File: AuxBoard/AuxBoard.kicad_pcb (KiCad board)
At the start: 2 copper layers, 85.2 x 59.2 mm, 29 parts, among them J1 ATX-24, J10 MatBIn, J11 FanHeader, J2 RPI4B, J4 MatrixASupply, J5 MatrixBSupply, J6 BigLED, J7 MatAOut, J8 MatAIn, J9 MatBOut, Q1 DMMT5401, Q2 DMG2305UX, Q3 DMG2305UX, Q4 DMG2305UX, SW1 SW_DPST, U1 74AHC04

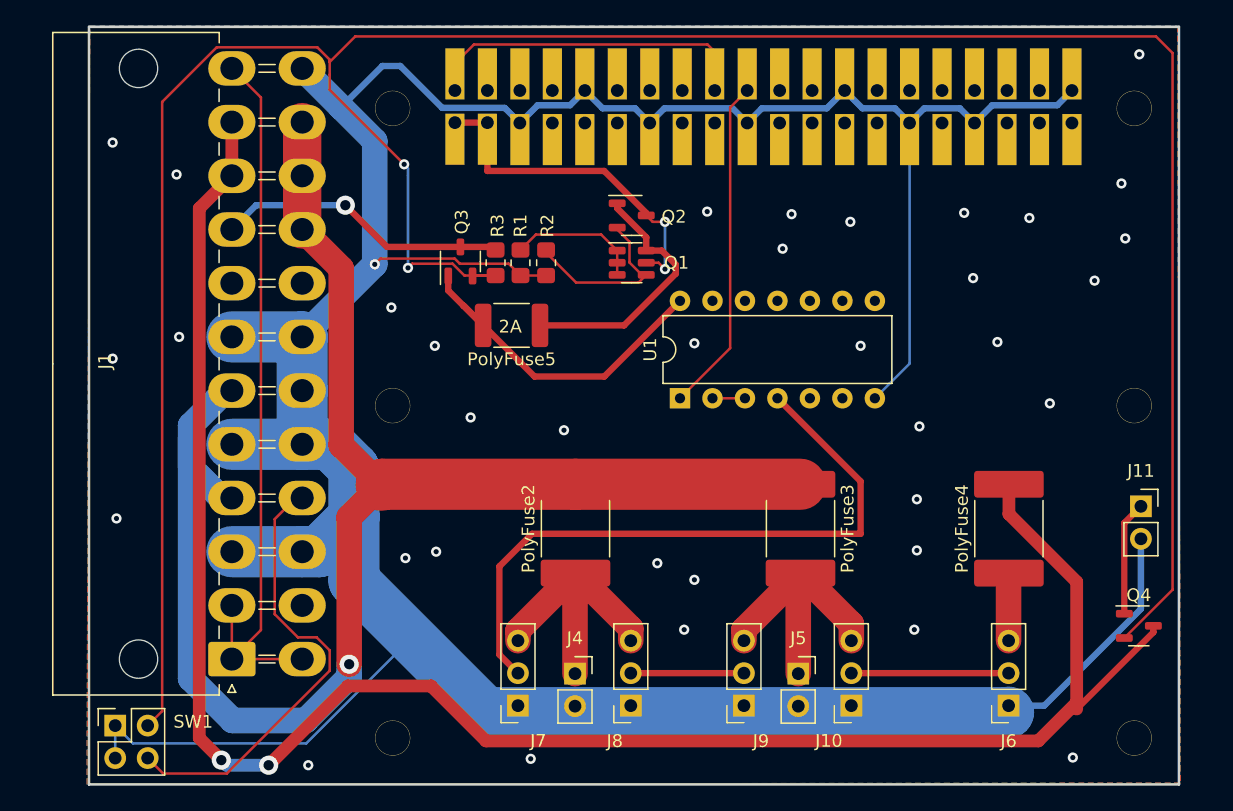
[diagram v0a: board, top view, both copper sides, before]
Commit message: Added Silkscreen
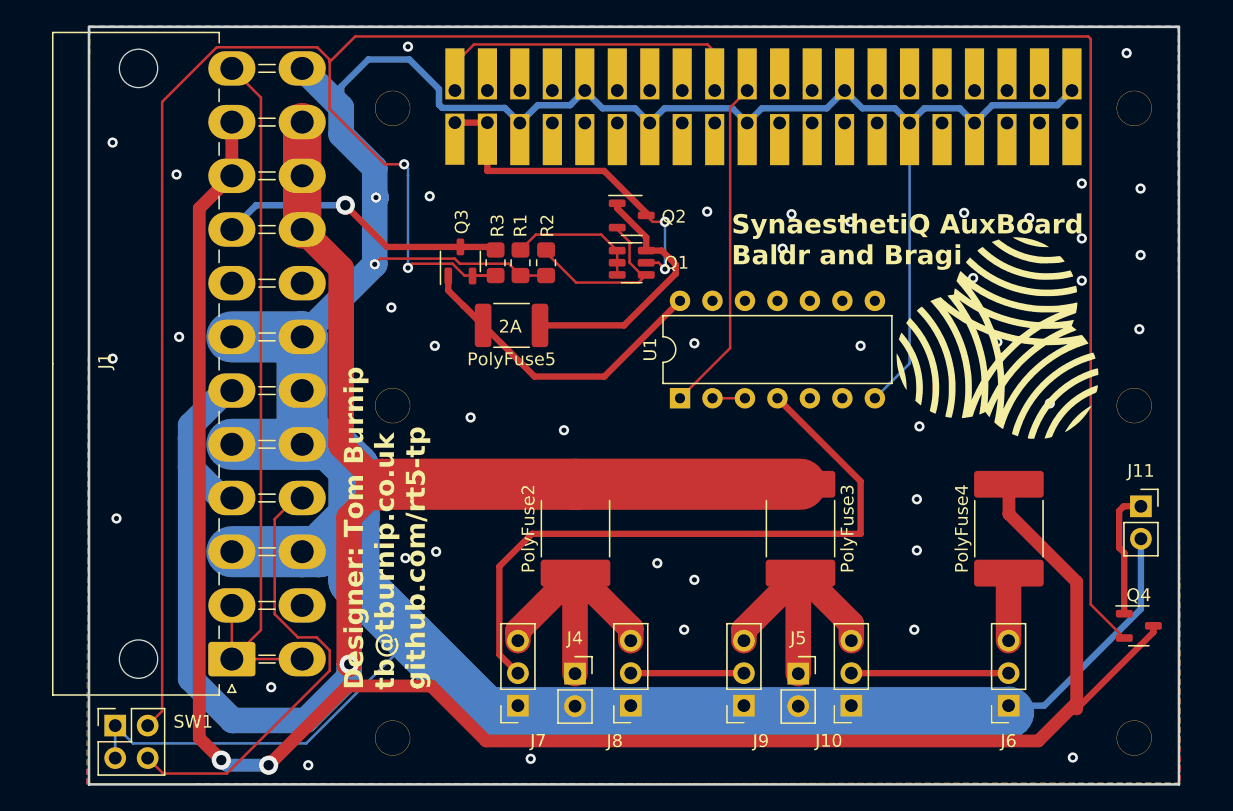
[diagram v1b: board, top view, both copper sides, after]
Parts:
- added G***: LOGO, RTEP:RTEPLogo, F.Cu at (175.8, 74.1)
- added G***: LOGO, RTEP:RTEPLogo, B.Cu at (175.5, 77.1)
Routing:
- net /5VSwitch: track 207.1 -> 201.8 mm
- net GND: track 278.1 -> 280.2 mm, vias 37 -> 44
- net Net-(J11-Pin_1): track 8.94 -> 10.1 mm
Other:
- board text added: "Designer: Tom Burnip tb@tburnip.co.uk github.com/rt5-tp"
- board text added: "SynaesthetiQ AuxBoard Baldr and Bragi"
- board text added: "SynaesthetiQ AuxBoard Baldr and Bragi Designer: Tom Burnip (tb@tburnip.co.uk) GitHub: https://github.com/rt5-tp"

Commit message: Gerbers for PCB. Fixed RPI Header Mistake. PCB will need bodge.
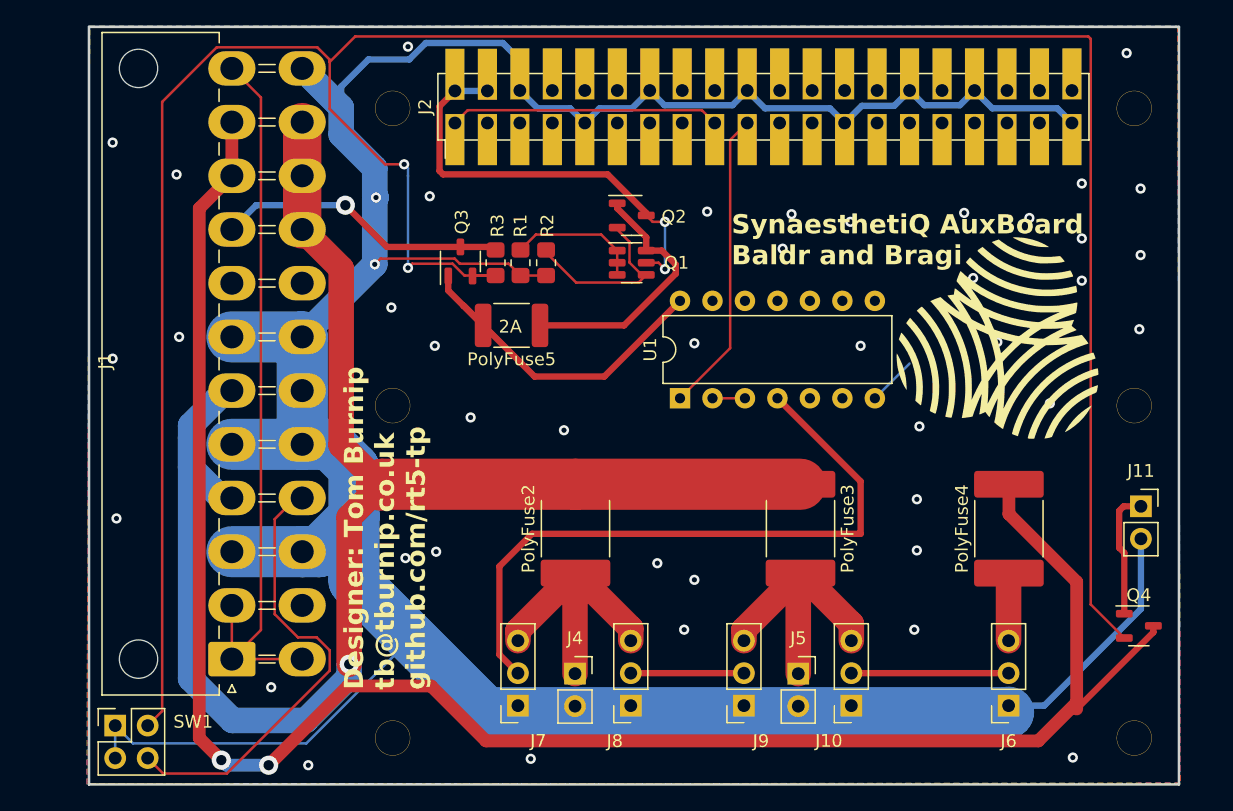
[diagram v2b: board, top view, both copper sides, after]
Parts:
- J1: footprint Connector_Molex:Molex_Mini-Fit_Jr_5569-24A2_2x12_P4.20mm_Horizontal -> Tom's Parts:Molex_Mini-Fit_Jr_5569-24A2_2x12_P4.20mm_Horizontal
- J2: moved to F.Cu
- turned J2 to 90 degrees
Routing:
- net GND: track 280.2 -> 262.1 mm
- net /5V_Power: track 27.3 -> 34.1 mm
- net /3V3_Power: track 26.3 -> 21.1 mm
- net /MOSI: track 26.2 -> 23.7 mm

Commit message: Fixing Header Orientation
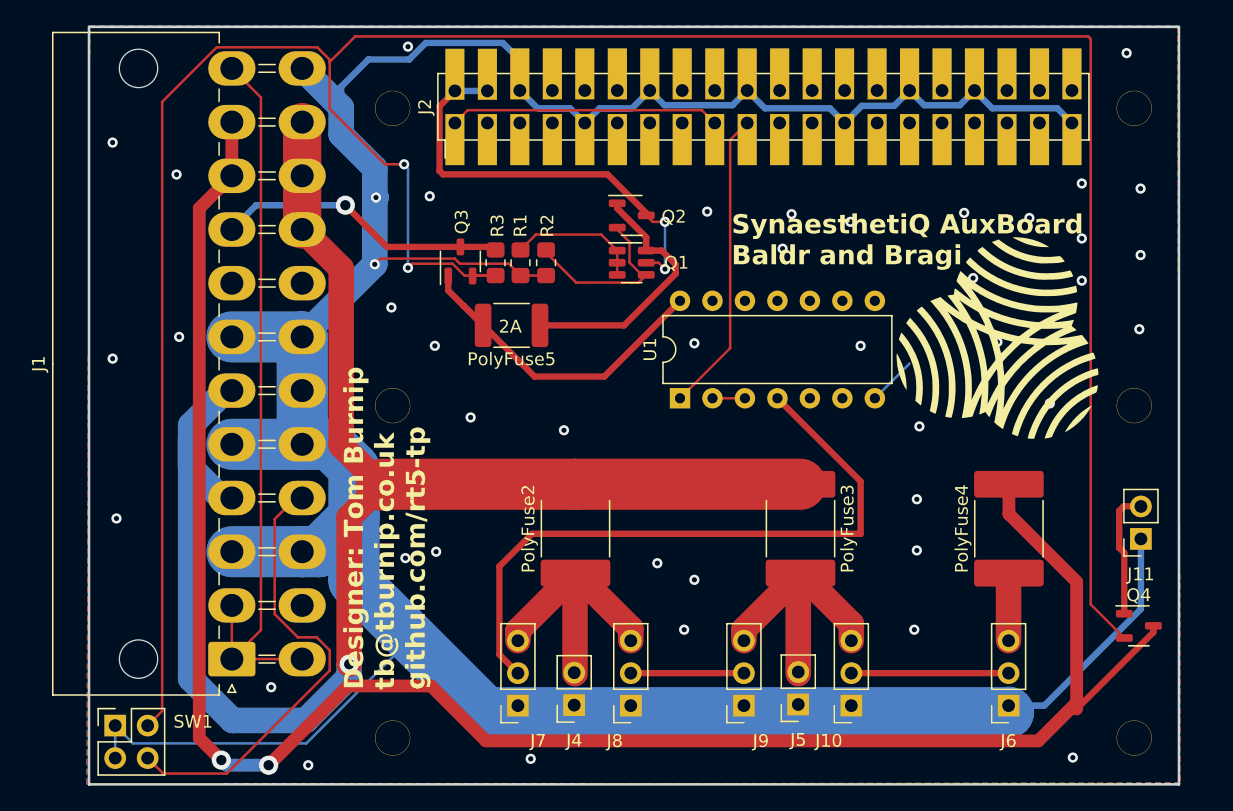
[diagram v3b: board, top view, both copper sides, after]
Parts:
- J1: footprint Tom's Parts:Molex_Mini-Fit_Jr_5569-24A2_2x12_P4.20mm_Horizontal -> Connector_Molex:Molex_Mini-Fit_Jr_5569-24A2_2x12_P4.20mm_Horizontal
- moved J11 2.55 mm to (187.0, 89.8), turned to 180 degrees
- moved J4 2.46 mm to (142.7, 102.8), turned to 180 degrees
- moved J5 2.41 mm to (160.2, 102.8), turned to 180 degrees
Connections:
- J11 pad 1: Net-(J11-Pin_1) -> GND
- J11 pad 2: GND -> Net-(J11-Pin_2)
- J4 pad 1: 5VMatA -> GND
- J4 pad 2: GND -> 5VMatA
- J5 pad 1: 5VMatB -> GND
- J5 pad 2: GND -> 5VMatB
- Q4 pad 1: Net-(J11-Pin_1) -> Net-(J11-Pin_2)
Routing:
- net Net-(J11-Pin_2): track 0.00 -> 10.1 mm
- net Net-(J11-Pin_1): track 10.1 -> 0.00 mm
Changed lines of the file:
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@@
   (net 48 "GND")
   (net 49 "+5VP")
-  (net 50 "Net-(J11-Pin_1)")
+  (net 50 "Net-(J11-Pin_2)")
   (net 51 "unconnected-(U1-Pad8)")
   (net 52 "unconnected-(U1-Pad9)")
@@
     )
   )
-  (footprint "Tom's Parts:Molex_Mini-Fit_Jr_5569-24A2_2x12_P4.20mm_Horizontal" (layer "F.Cu")
+  (footprint "Connector_Molex:Molex_Mini-Fit_Jr_5569-24A2_2x12_P4.20mm_Horizontal" (layer "F.Cu")
     (at 115.925 99.2 90)
     (descr "Molex Mini-Fit Jr. Power Connectors, old mpn/engineering number: 5569-24A2, example for new mpn: 39-30-0240, 12 Pins per row, Mounting: Snap-in Plastic Peg PCB Lock (http://www.molex.com/pdm_docs/sd/039300020_sd.pdf), generated with kicad-footprint-generator")
@@
     (property "ki_keywords" "ATX PSU")
     (attr through_hole)
-    (fp_text reference "J1" (at 23.3 -9.925 90) (layer "F.SilkS")
+    (fp_text reference "J1" (at 23.1 -15.1 90) (layer "F.SilkS")
         (effects (font (size 1 1) (thickness 0.15)))
     )
@@
         (effects (font (size 1 1) (thickness 0.15)))
     )
-    (fp_text user "${REFERENCE}" (at 23.6 -8.525 90) (layer "F.Fab")
+    (fp_text user "${REFERENCE}" (at 23.1 -13.2 90) (layer "F.Fab")
         (effects (font (size 1 1) (thickness 0.15)))
     )
-    (fp_line (start -2.81 -10.16) (end 23.1 -10.16)
+    (fp_line (start -2.81 -14.01) (end 23.1 -14.01)
       (stroke (width 0.12) (type solid)) (layer "F.SilkS"))
-    (fp_line (start -2.81 -0.99) (end -2.81 -10.16)
+    (fp_line (start -2.81 -0.99) (end -2.81 -14.01)
       (stroke (width 0.12) (type solid)) (layer "F.SilkS"))
     (fp_line (start -2.6 -0.3) (end -2 0)
@@
     (fp_line (start 48.2 -0.99) (end 49.01 -0.99)
       (stroke (width 0.12) (type solid)) (layer "F.SilkS"))
-    (fp_line (start 49.01 -10.16) (end 23.1 -10.16)
+    (fp_line (start 49.01 -14.01) (end 23.1 -14.01)
       (stroke (width 0.12) (type solid)) (layer "F.SilkS"))
-    (fp_line (start 49.01 -0.99) (end 49.01 -10.16)
+    (fp_line (start 49.01 -0.99) (end 49.01 -14.01)
       (stroke (width 0.12) (type solid)) (layer "F.SilkS"))
     (fp_line (start -3.2 -14.4) (end -3.2 7.85)
@@
     (fp_line (start 49.4 7.85) (end 49.4 -14.4)
       (stroke (width 0.05) (type solid)) (layer "F.CrtYd"))
-    (fp_line (start -2.7 -10.16) (end -2.7 -1.1)
+    (fp_line (start -2.7 -13.9) (end -2.7 -1.1)
       (stroke (width 0.1) (type solid)) (layer "F.Fab"))
     (fp_line (start -2.7 -1.1) (end 48.9 -1.1)
@@
     (fp_line (start 0 -2.514214) (end 1 -1.1)
       (stroke (width 0.1) (type solid)) (layer "F.Fab"))
-    (fp_line (start 48.9 -10.16) (end -2.7 -10.16)
+    (fp_line (start 48.9 -13.9) (end -2.7 -13.9)
       (stroke (width 0.1) (type solid)) (layer "F.Fab"))
-    (fp_line (start 48.9 -1.1) (end 48.9 -10.16)
+    (fp_line (start 48.9 -1.1) (end 48.9 -13.9)
       (stroke (width 0.1) (type solid)) (layer "F.Fab"))
     (pad "" np_thru_hole circle (at 0 -7.3 90) (size 3 3) (drill 3) (layers "*.Cu" "*.Mask"))
     (pad "" np_thru_hole circle (at 46.2 -7.3 90) (size 3 3) (drill 3) (layers "*.Cu" "*.Mask"))
-    (pad "1" thru_hole roundrect (at 0 0 90) (size 2.7 3.7) (drill 1.8) (layers "*.Cu" "*.Mask") (roundrect_rratio 0.09259296296)
+    (pad "1" thru_hole roundrect (at 0 0 90) (size 2.7 3.7) (drill 1.8) (layers "*.Cu" "*.Mask") (roundrect_rratio 0.092593)
       (net 47 "+3.3V") (pinfunction "+3.3V") (pintype "power_out"))
     (pad "2" thru_hole oval (at 4.2 0 90) (size 2.7 3.7) (drill 1.8) (layers "*.Cu" "*.Mask")
@@
   )
   (footprint "Connector_PinSocket_2.54mm:PinSocket_1x02_P2.54mm_Vertical" (layer "F.Cu")
-    (at 142.7625 100.34)
+    (at 142.7 102.8 180)
     (descr "Through hole straight socket strip, 1x02, 2.54mm pitch, single row (from Kicad 4.0.7), script generated")
     (tags "Through hole socket strip THT 1x02 2.54mm single row")
@@
     (fp_line (start 1.27 3.81) (end -1.27 3.81)
       (stroke (width 0.1) (type solid)) (layer "F.Fab"))
-    (pad "1" thru_hole rect (at 0 0) (size 1.7 1.7) (drill 1) (layers "*.Cu" "*.Mask")
-      (net 44 "5VMatA") (pinfunction "Pin_1") (pintype "passive"))
-    (pad "2" thru_hole oval (at 0 2.54) (size 1.7 1.7) (drill 1) (layers "*.Cu" "*.Mask")
-      (net 48 "GND") (pinfunction "Pin_2") (pintype "passive"))
+    (pad "1" thru_hole rect (at 0 0 180) (size 1.7 1.7) (drill 1) (layers "*.Cu" "*.Mask")
+      (net 48 "GND") (pinfunction "Pin_1") (pintype "passive"))
+    (pad "2" thru_hole oval (at 0 2.54 180) (size 1.7 1.7) (drill 1) (layers "*.Cu" "*.Mask")
+      (net 44 "5VMatA") (pinfunction "Pin_2") (pintype "passive"))
     (model "${KICAD6_3DMODEL_DIR}/Connector_PinSocket_2.54mm.3dshapes/PinSocket_1x02_P2.54mm_Vertical.wrl"
       (offset (xyz 0 0 0))
@@
   )
   (footprint "Connector_PinSocket_2.54mm:PinSocket_1x02_P2.54mm_Vertical" (layer "F.Cu")
-    (at 160.225 100.34)
+    (at 160.225 102.75 180)
     (descr "Through hole straight socket strip, 1x02, 2.54mm pitch, single row (from Kicad 4.0.7), script generated")
     (tags "Through hole socket strip THT 1x02 2.54mm single row")
@@
     (fp_line (start 1.27 3.81) (end -1.27 3.81)
       (stroke (width 0.1) (type solid)) (layer "F.Fab"))
-    (pad "1" thru_hole rect (at 0 0) (size 1.7 1.7) (drill 1) (layers "*.Cu" "*.Mask")
-      (net 46 "5VMatB") (pinfunction "Pin_1") (pintype "passive"))
-    (pad "2" thru_hole oval (at 0 2.54) (size 1.7 1.7) (drill 1) (layers "*.Cu" "*.Mask")
-      (net 48 "GND") (pinfunction "Pin_2") (pintype "passive"))
+    (pad "1" thru_hole rect (at 0 0 180) (size 1.7 1.7) (drill 1) (layers "*.Cu" "*.Mask")
+      (net 48 "GND") (pinfunction "Pin_1") (pintype "passive"))
+    (pad "2" thru_hole oval (at 0 2.54 180) (size 1.7 1.7) (drill 1) (layers "*.Cu" "*.Mask")
+      (net 46 "5VMatB") (pinfunction "Pin_2") (pintype "passive"))
     (model "${KICAD6_3DMODEL_DIR}/Connector_PinSocket_2.54mm.3dshapes/PinSocket_1x02_P2.54mm_Vertical.wrl"
       (offset (xyz 0 0 0))
@@
   )
   (footprint "Connector_PinSocket_2.54mm:PinSocket_1x02_P2.54mm_Vertical" (layer "F.Cu")
-    (at 187.025 87.25)
+    (at 187.025 89.8 180)
     (descr "Through hole straight socket strip, 1x02, 2.54mm pitch, single row (from Kicad 4.0.7), script generated")
     (tags "Through hole socket strip THT 1x02 2.54mm single row")
@@
     (fp_line (start 1.27 3.81) (end -1.27 3.81)
       (stroke (width 0.1) (type solid)) (layer "F.Fab"))
-    (pad "1" thru_hole rect (at 0 0) (size 1.7 1.7) (drill 1) (layers "*.Cu" "*.Mask")
-      (net 50 "Net-(J11-Pin_1)") (pinfunction "Pin_1") (pintype "passive"))
-    (pad "2" thru_hole oval (at 0 2.54) (size 1.7 1.7) (drill 1) (layers "*.Cu" "*.Mask")
-      (net 48 "GND") (pinfunction "Pin_2") (pintype "passive"))
+    (pad "1" thru_hole rect (at 0 0 180) (size 1.7 1.7) (drill 1) (layers "*.Cu" "*.Mask")
+      (net 48 "GND") (pinfunction "Pin_1") (pintype "passive"))
+    (pad "2" thru_hole oval (at 0 2.54 180) (size 1.7 1.7) (drill 1) (layers "*.Cu" "*.Mask")
+      (net 50 "Net-(J11-Pin_2)") (pinfunction "Pin_2") (pintype "passive"))
     (model "${KICAD6_3DMODEL_DIR}/Connector_PinSocket_2.54mm.3dshapes/PinSocket_1x02_P2.54mm_Vertical.wrl"
       (offset (xyz 0 0 0))
@@
       (stroke (width 0.1) (type solid)) (layer "F.Fab"))
     (pad "1" smd roundrect (at -1.1375 -0.95) (size 1.325 0.6) (layers "F.Cu" "F.Paste" "F.Mask") (roundrect_rratio 0.25)
-      (net 50 "Net-(J11-Pin_1)") (pinfunction "D") (pintype "passive"))
+      (net 50 "Net-(J11-Pin_2)") (pinfunction "D") (pintype "passive"))
     (pad "2" smd roundrect (at -1.1375 0.95) (size 1.325 0.6) (layers "F.Cu" "F.Paste" "F.Mask") (roundrect_rratio 0.25)
       (net 60 "/5VSwitch") (pinfunction "G") (pintype "input"))

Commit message: Updates to the Aux Board PCB
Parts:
- moved J11 4.30 mm to (187.1, 94.1)
- moved Q4 1.89 mm to (185.6, 98.0), turned to 90 degrees
- moved Q3 0.45 mm to (133.4, 67.9), turned to 180 degrees
- moved Q2 0.28 mm to (147.0, 64.3), turned to -90 degrees
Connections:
- Q2 pad 1: Net-(Q1A-E1) -> Net-(Q1B-C2)
- Q2 pad 2: Net-(Q1B-C2) -> /5V_Power
- Q2 pad 3: /5V_Power -> Net-(Q1A-E1)
- Q3 pad 1: +5VP -> /5VSwitch
- Q3 pad 2: /5VSwitch -> 5VSB
- Q3 pad 3: 5VSB -> +5VP
- Q4 pad 1: Net-(J11-Pin_2) -> /5VSwitch
- Q4 pad 2: /5VSwitch -> +12V
- Q4 pad 3: +12V -> Net-(J11-Pin_2)
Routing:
- net Net-(J11-Pin_2): track 10.1 -> 5.92 mm
- net +12V: track 153.1 -> 149.6 mm
- net GND: track 262.1 -> 258.6 mm
- net /5V_Power: track 34.1 -> 37.1 mm
- net Net-(Q1B-C2): track 14.1 -> 16.9 mm
- net Net-(Q1A-E1): track 20.4 -> 18.1 mm
- net +5VP: track 26.7 -> 28.3 mm

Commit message: update
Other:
- board text added: "SynaesthetiQ AuxBoard 1.1 Baldr and Bragi"
- board text added: "SynaesthetiQ AuxBoard 1.1 Baldr and Bragi Designer: Tom Burnip (tb@tburnip.co.uk) GitHub: https://github.com/rt5-tp"
- board text removed: "SynaesthetiQ AuxBoard Baldr and Bragi"
- board text removed: "SynaesthetiQ AuxBoard Baldr and Bragi Designer: Tom Burnip (tb@tburnip.co.uk) GitHub: https://github.com/rt5-tp"
